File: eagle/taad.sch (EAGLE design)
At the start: 56 parts, among them IC1 LD117AS33TR, Q1 16 MHz, X1 MINI-USB-32005-201

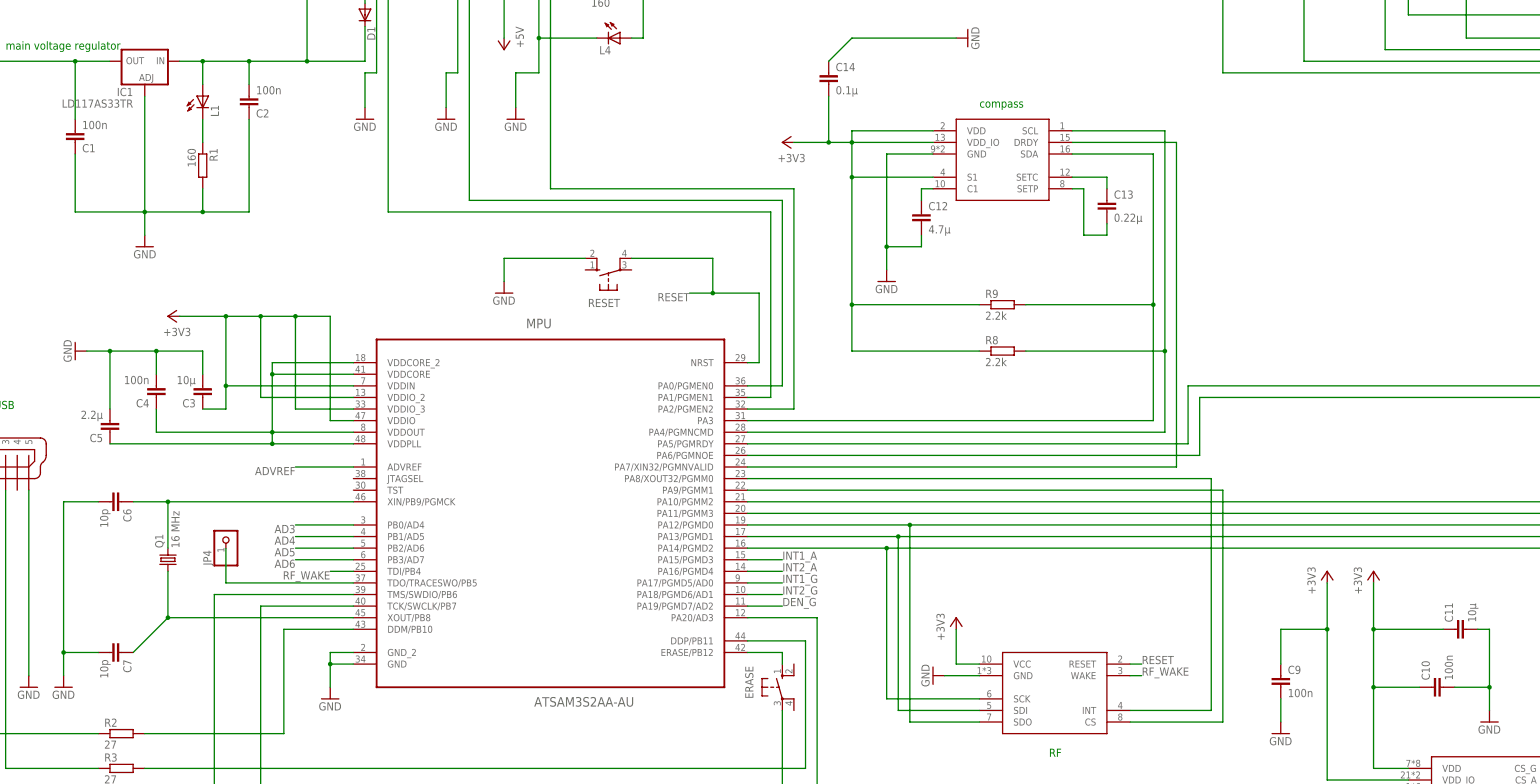
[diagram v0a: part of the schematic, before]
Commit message: Changed 100nF to 0.1µF (same value different marking)
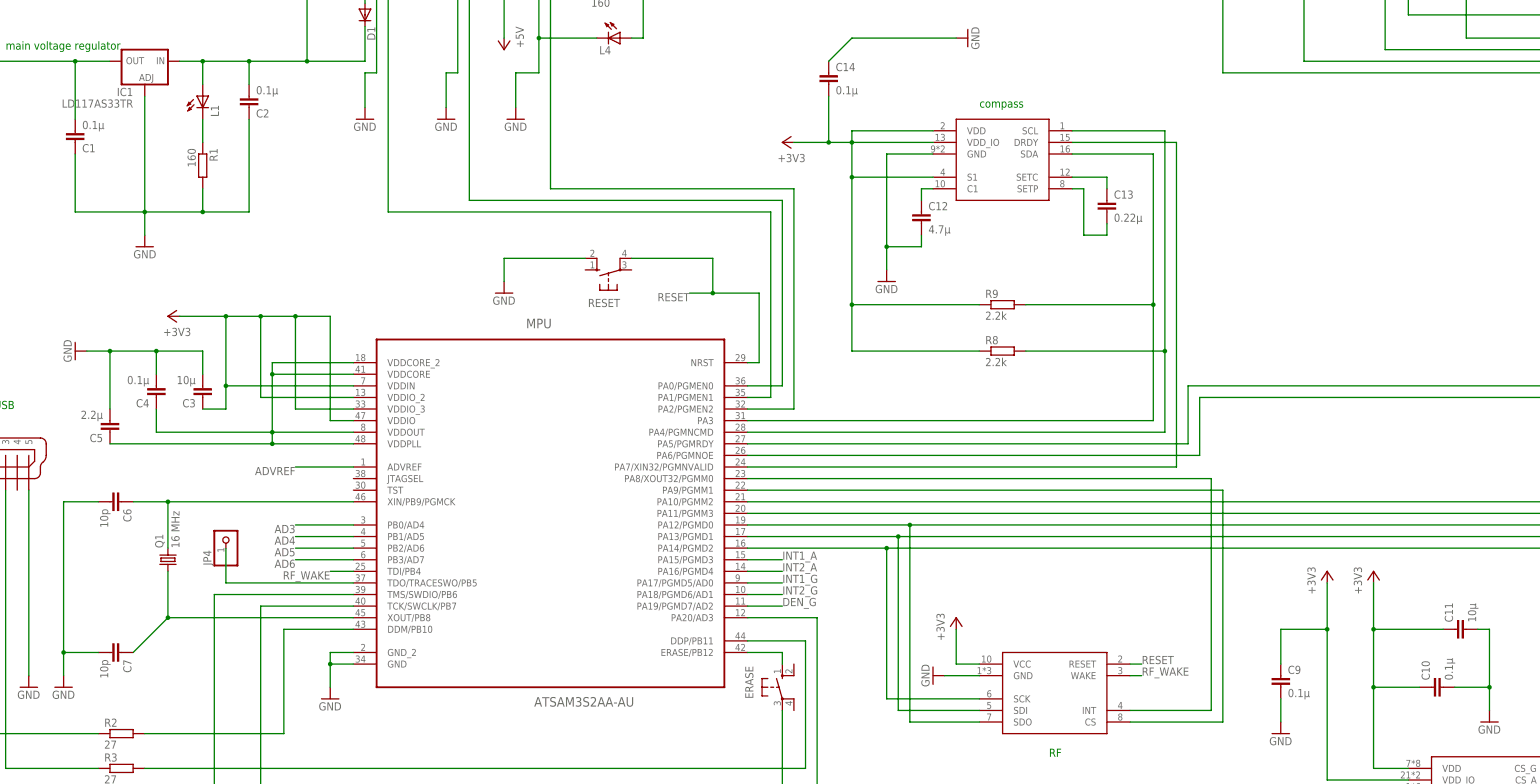
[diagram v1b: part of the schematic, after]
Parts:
- C1, C10, C2, C4, C9: value 100n -> 0.1µ
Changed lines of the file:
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@@
 <part name="IC1" library="v-reg" deviceset="LD117A?*" device="S" technology="33TR"/>
 <part name="GND3" library="supply1" deviceset="GND" device=""/>
-<part name="C2" library="resistor" deviceset="C-EU" device="C0805" value="100n"/>
-<part name="C1" library="resistor" deviceset="C-EU" device="C0805" value="100n"/>
+<part name="C2" library="resistor" deviceset="C-EU" device="C0805" value="0.1µ"/>
+<part name="C1" library="resistor" deviceset="C-EU" device="C0805" value="0.1µ"/>
 <part name="+3V1" library="supply1" deviceset="+3V3" device=""/>
 <part name="GND7" library="supply1" deviceset="GND" device=""/>
@@
 <part name="+3V3" library="supply1" deviceset="+3V3" device=""/>
 <part name="C11" library="rcl" deviceset="C-EU" device="C0805" value="10µ"/>
-<part name="C10" library="rcl" deviceset="C-EU" device="C0805" value="100n"/>
+<part name="C10" library="rcl" deviceset="C-EU" device="C0805" value="0.1µ"/>
 <part name="GND10" library="supply1" deviceset="GND" device=""/>
 <part name="+3V7" library="supply1" deviceset="+3V3" device=""/>
-<part name="C9" library="rcl" deviceset="C-EU" device="C0805" value="100n"/>
+<part name="C9" library="rcl" deviceset="C-EU" device="C0805" value="0.1µ"/>
 <part name="GND12" library="supply1" deviceset="GND" device=""/>
 <part name="I/O-PWM" library="max696x" deviceset="MAX6967AEE" device=""/>
@@
 <part name="GND20" library="supply1" deviceset="GND" device=""/>
 <part name="+3V9" library="supply1" deviceset="+3V3" device=""/>
-<part name="C4" library="rcl" deviceset="C-EU" device="C0805" value="100n"/>
+<part name="C4" library="rcl" deviceset="C-EU" device="C0805" value="0.1µ"/>
 <part name="GND9" library="supply1" deviceset="GND" device=""/>
 <part name="+3V2" library="supply1" deviceset="+3V3" device=""/>
